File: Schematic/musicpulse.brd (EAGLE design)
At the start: 70.8 x 48.2 mm, 19 parts, among them IC1 UA78M33DCY

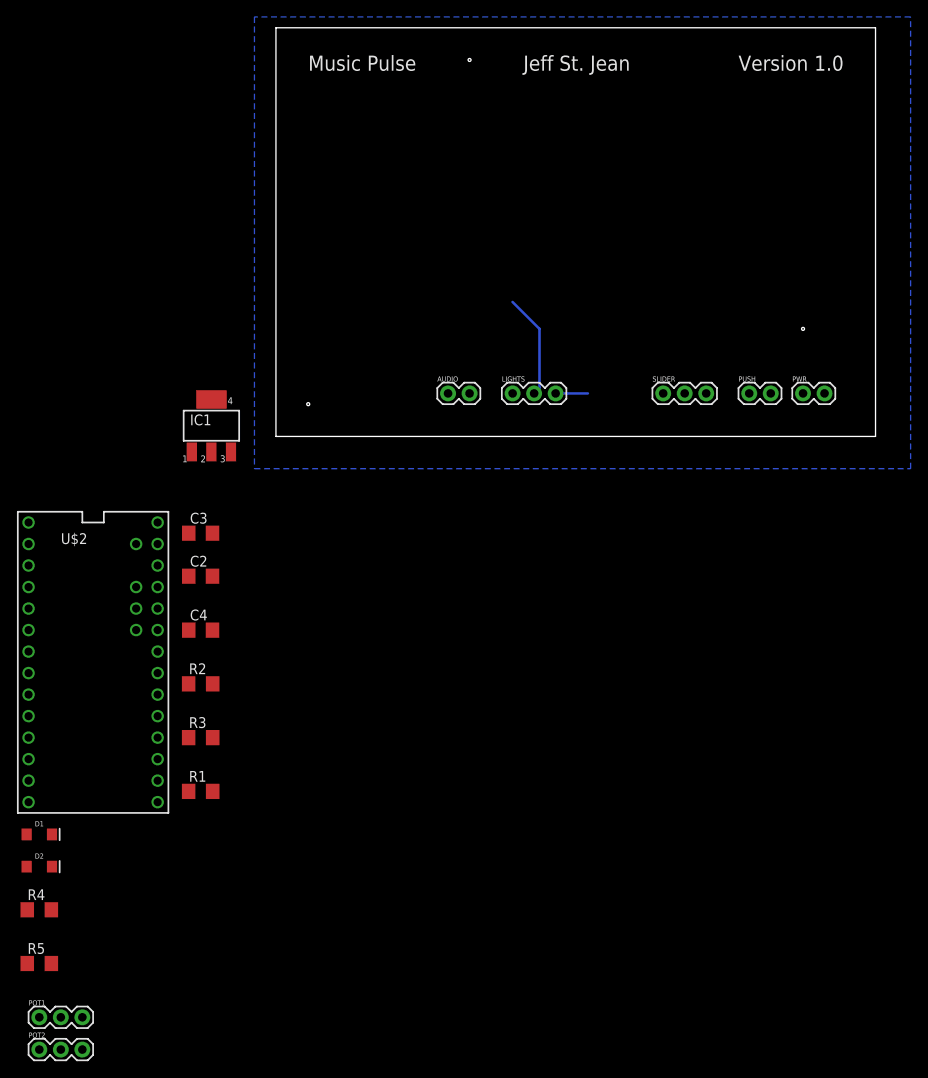
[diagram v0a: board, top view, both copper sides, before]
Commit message: Changed to through hole. Adjusted some resistor files. Rerouted board. Reprocessed gerbers. Added board and schematic reference pictures.
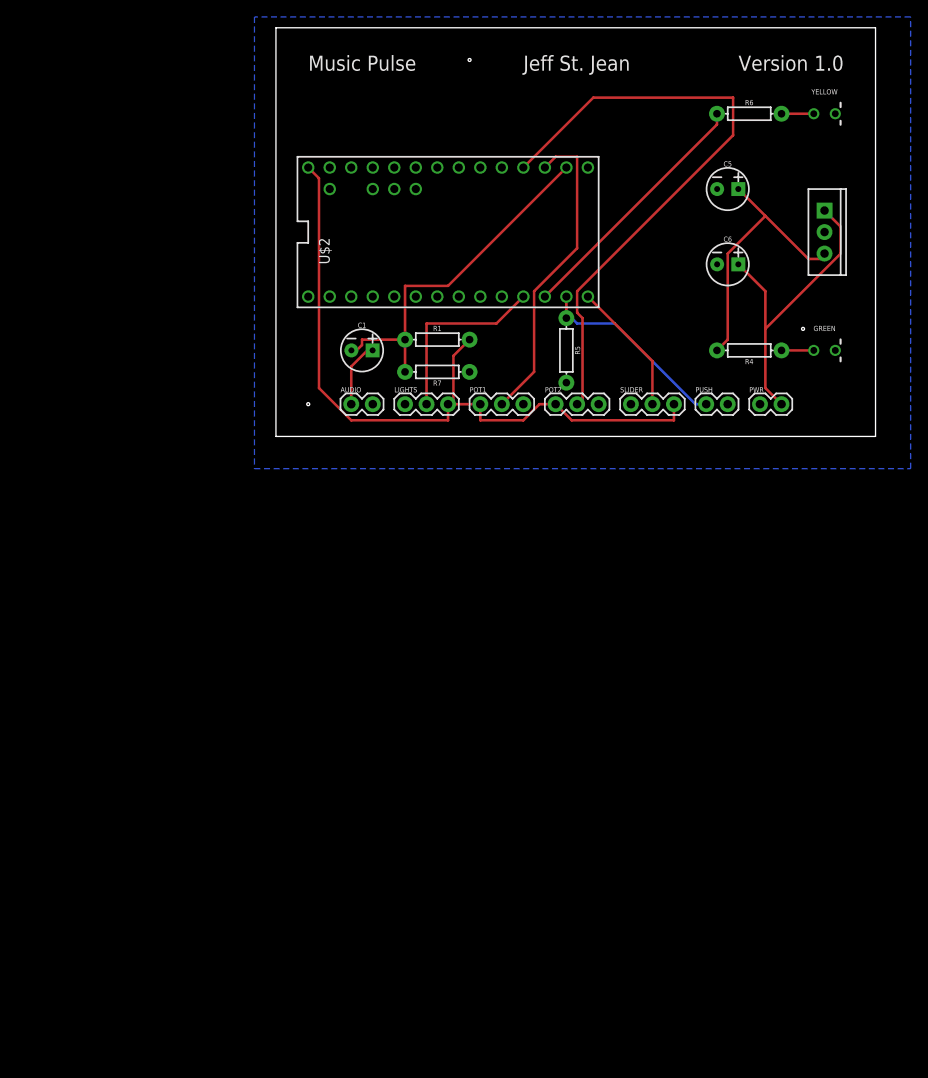
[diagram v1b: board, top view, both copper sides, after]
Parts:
- removed C2: 0.1uF, BeagleBone_Black_Wireless:C1206
- removed C3: 0.33uF, BeagleBone_Black_Wireless:C1206
- removed C4: 10uF, BeagleBone_Black_Wireless:C1206
- removed D1: GREEN, SparkFun-LED:LED-1206
- removed D2: Yellow, SparkFun-LED:LED-1206
- removed IC1: UA78M33DCY, linear:SOT223
- removed R2, R3: 10k, BeagleBone_Black_Wireless:R1206
- added C1: 1uF, SparkFun-Capacitors:CPOL-RADIAL-2.5MM-5MM
- added C5: 0.33uF, SparkFun-Capacitors:CPOL-RADIAL-2.5MM-5MM
- added C6: 0.1uF, SparkFun-Capacitors:CPOL-RADIAL-2.5MM-5MM
- added GREEN, YELLOW: (no value), SparkFun-LED:LED_3MM-NS
- added R6: 100, SparkFun-Resistors:AXIAL-0.3
- added R7: 10K, SparkFun-Resistors:AXIAL-0.3
- added UA7805C: (no value), SparkFun-IC-Power:TO220-IGO
- R1: value 10k -> 4.3K; device BeagleBone_Black_Wireless:R1206 -> SparkFun-Resistors:AXIAL-0.3
- R4: device BeagleBone_Black_Wireless:R1206 -> SparkFun-Resistors:AXIAL-0.3
- R5: value 100 -> 10K; device BeagleBone_Black_Wireless:R1206 -> SparkFun-Resistors:AXIAL-0.3
- moved R4 106.7 mm to (55.9, 10.2), turned to 180 degrees
- moved POT2 97.6 mm to (33.0, 3.81)
- moved R5 95.5 mm to (34.3, 10.2), turned to 270 degrees
- moved POT1 89.2 mm to (24.1, 3.81)
- moved U$2 65.9 mm to (20.3, 24.1), turned to 90 degrees
- moved R1 60.2 mm to (19.1, 11.4)
- moved LIGHTS 12.8 mm to (15.2, 3.81)
- moved AUDIO 11.5 mm to (8.89, 3.81)
- moved PUSH 5.24 mm to (50.8, 3.81)
- moved PWR 5.24 mm to (57.1, 3.81)
- moved SLIDER 4.02 mm to (41.9, 3.81)
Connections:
- net AUDIO_IN: now also C1.2, R1.P$1, R7.P$2; no longer C4.1, R2.2, R3.1
- net GND: now also C5.2, C6.2, GREEN.K, R7.P$1, UA7805C.GND, YELLOW.K; no longer C2.2, C3.2, D1.C, D2.C, IC1.2, IC1.4, R2.1
- net LED_GREEN: now also C5.1, R4.P$2, UA7805C.OUT; no longer C3.1, IC1.3, R4.1
- net LED_YELLOW: now also R6.P$1; no longer R5.2
- net N$1: now also C6.1, UA7805C.IN; no longer C2.1, IC1.1
- net N$2: now also R6.P$2, YELLOW.A; no longer D1.A, R4.2
- net N$3: now also R5.P$2; no longer R1.2
- net N$4: now also GREEN.A, R4.P$1; no longer D2.A, R5.1
- net N$5: now also C1.1; no longer C4.2
- net PUSH: now also R5.P$1; no longer R1.1
- net VCC: now also R1.P$2; no longer R3.2
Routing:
- net VCC: track 3.81 -> 85.8 mm
- net POT2: track 0.00 -> 72.5 mm
- net AUDIO_IN: track 0.00 -> 42.2 mm
- net POT1: track 0.00 -> 37.2 mm
- net N$1: track 0.00 -> 37.1 mm
- net LED_GREEN: track 0.00 -> 32.5 mm
- net LED_YELLOW: track 0.00 -> 30.0 mm
- net PUSH: track 0.00 -> 23.3 mm
- net SLIDE: track 0.00 -> 15.9 mm
- net LIGHTS: track 12.4 -> 22.3 mm
- net N$5: track 0.00 -> 7.75 mm
- net N$4: track 0.00 -> 3.81 mm
- net N$2: track 0.00 -> 3.81 mm

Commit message: Rerouted board. Added pullup to slider. Changed some resistor values.
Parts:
- removed C5: 0.33uF, SparkFun-Capacitors:CPOL-RADIAL-2.5MM-5MM
- added C3: 1uF, SparkFun-Capacitors:CPOL-RADIAL-2.5MM-5MM
- added R3: 330, SparkFun-Resistors:AXIAL-0.3
- C1: value 1uF -> 0.1uF
- C2: value 0.1uF -> 0.33uF
- R4: value 100 -> 330
- R6: value 100 -> 10K
- U$2: value TEENSY_3.1-3.2_DIL+4 -> TEENSY_3.2
- moved C1 46.7 mm to (53.3, 27.9)
- moved PWR 29.6 mm to (52.1, 33.0)
- moved R6 28.1 mm to (48.4, 11.0), turned to 270 degrees
- moved YELLOW 27.9 mm to (45.7, 17.8), turned to 180 degrees
- moved R4 15.8 mm to (46.6, 23.0), turned to 0 degrees
- moved PUSH 8.89 mm to (41.9, 3.81)
- moved SLIDER 6.35 mm to (48.3, 3.81)
- turned R5 to 180 degrees
- renumbered C6 to C2, R7 to R2
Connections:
- removed net LED_GREEN: C5.1, R4.P$2, UA7805C.OUT
- net AUDIO_IN: now also C3.2; no longer C1.2
- net GND: now also C1.2; no longer C5.2
- net LED_YELLOW: now also R4.P$1; no longer R6.P$1
- net N$1: now also C1.1; no longer C2.1
- net N$2: now also R4.P$2; no longer R6.P$2
- net N$4: now also R3.P$1; no longer R4.P$1
- net N$5: now also C3.1; no longer C1.1
- net SLIDE: now also R6.P$2
- net VCC: now also C2.1, R3.P$2, R6.P$1, UA7805C.OUT
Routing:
- net VCC: track 85.8 -> 125.4 mm
- net LED_GREEN: track 32.5 -> 0.00 mm
- net AUDIO_IN: track 42.2 -> 68.0 mm
- net N$1: track 37.1 -> 15.8 mm
- net LED_YELLOW: track 30.0 -> 13.7 mm
- net POT1: track 37.2 -> 45.5 mm
- net SLIDE: track 15.9 -> 23.7 mm
- net PUSH: track 23.3 -> 15.9 mm
- net N$2: track 3.81 -> 6.63 mm
- net LIGHTS: track 22.3 -> 19.6 mm
- net N$5: track 7.75 -> 6.36 mm
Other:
- board size 70.8 x 48.2 mm -> 70.8 x 41.9 mm
- board text added: "Music Kaleidoscope"
- board text removed: "Music Pulse"

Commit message: Added missing trace. Reprocessed CAM files.
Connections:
- removed net N$3: R5.P$2
- net VCC: now also R5.P$2
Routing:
- net VCC: track 125.4 -> 131.5 mm
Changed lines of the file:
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@@
 </element>
 <element name="R4" library="SparkFun-Resistors" library_urn="urn:adsk.eagle:library:532" package="AXIAL-0.3" package3d_urn="urn:adsk.eagle:package:39658/1" value="330" x="46.609" y="22.987" smashed="yes">
-<attribute name="NAME" x="46.609" y="24.003" size="0.6096" layer="25" font="vector" ratio="20" align="bottom-center"/>
+<attribute name="NAME" x="46.609" y="21.463" size="0.6096" layer="25" font="vector" ratio="20" align="bottom-center"/>
 <attribute name="PROD_ID" value="RES-12182" x="46.609" y="22.987" size="1.778" layer="27" display="off"/>
-<attribute name="VALUE" x="46.609" y="21.971" size="0.6096" layer="27" font="vector" ratio="20" align="top-center"/>
+<attribute name="VALUE" x="46.609" y="24.511" size="0.6096" layer="27" font="vector" ratio="20" align="top-center"/>
 </element>
 <element name="R3" library="SparkFun-Resistors" library_urn="urn:adsk.eagle:library:532" package="AXIAL-0.3" package3d_urn="urn:adsk.eagle:package:39658/1" value="330" x="55.88" y="10.16" smashed="yes" rot="R180">
@@
 </element>
 <element name="R1" library="SparkFun-Resistors" library_urn="urn:adsk.eagle:library:532" package="AXIAL-0.3" package3d_urn="urn:adsk.eagle:package:39658/1" value="4.3K" x="19.05" y="11.43" smashed="yes">
-<attribute name="NAME" x="19.05" y="12.446" size="0.6096" layer="25" font="vector" ratio="20" align="bottom-center"/>
+<attribute name="NAME" x="19.05" y="9.906" size="0.6096" layer="25" font="vector" ratio="20" align="bottom-center"/>
 <attribute name="PROD_ID" value="RES-12182" x="19.05" y="11.43" size="1.778" layer="27" display="off"/>
-<attribute name="VALUE" x="19.05" y="10.414" size="0.6096" layer="27" font="vector" ratio="20" align="top-center"/>
+<attribute name="VALUE" x="19.05" y="12.954" size="0.6096" layer="27" font="vector" ratio="20" align="top-center"/>
 </element>
 <element name="R2" library="SparkFun-Resistors" library_urn="urn:adsk.eagle:library:532" package="AXIAL-0.3" package3d_urn="urn:adsk.eagle:package:39658/1" value="10K" x="19.05" y="7.62" smashed="yes" rot="R180">
@@
 <wire x1="22.86" y1="11.43" x2="24.13" y2="11.43" width="0.3048" layer="16"/>
 <wire x1="24.13" y1="11.43" x2="25.4" y2="10.16" width="0.3048" layer="16"/>
-<wire x1="25.4" y1="10.16" x2="25.4" y2="5.08" width="0.3048" layer="16"/>
+<wire x1="25.4" y1="10.16" x2="25.4" y2="7.62" width="0.3048" layer="16"/>
+<wire x1="25.4" y1="7.62" x2="25.4" y2="5.08" width="0.3048" layer="16"/>
 <wire x1="25.4" y1="5.08" x2="24.13" y2="3.81" width="0.3048" layer="16"/>
 <wire x1="22.86" y1="11.43" x2="20.32" y2="13.97" width="0.3048" layer="1"/>
@@
 <wire x1="48.387" y1="14.859" x2="49.149" y2="14.859" width="0.3048" layer="1"/>
 <wire x1="49.149" y1="14.859" x2="52.07" y2="17.78" width="0.3048" layer="1"/>
+<contactref element="R5" pad="P$2"/>
+<wire x1="30.48" y1="10.16" x2="27.94" y2="10.16" width="0.3048" layer="16"/>
+<wire x1="27.94" y1="10.16" x2="25.4" y2="7.62" width="0.3048" layer="16"/>
 </signal>
 <signal name="LIGHTS">
@@
 <wire x1="43.18" y1="20.32" x2="31.75" y2="31.75" width="0.3048" layer="1"/>
 </signal>
-<signal name="N$3">
-<contactref element="R5" pad="P$2"/>
-</signal>
 <signal name="N$2">

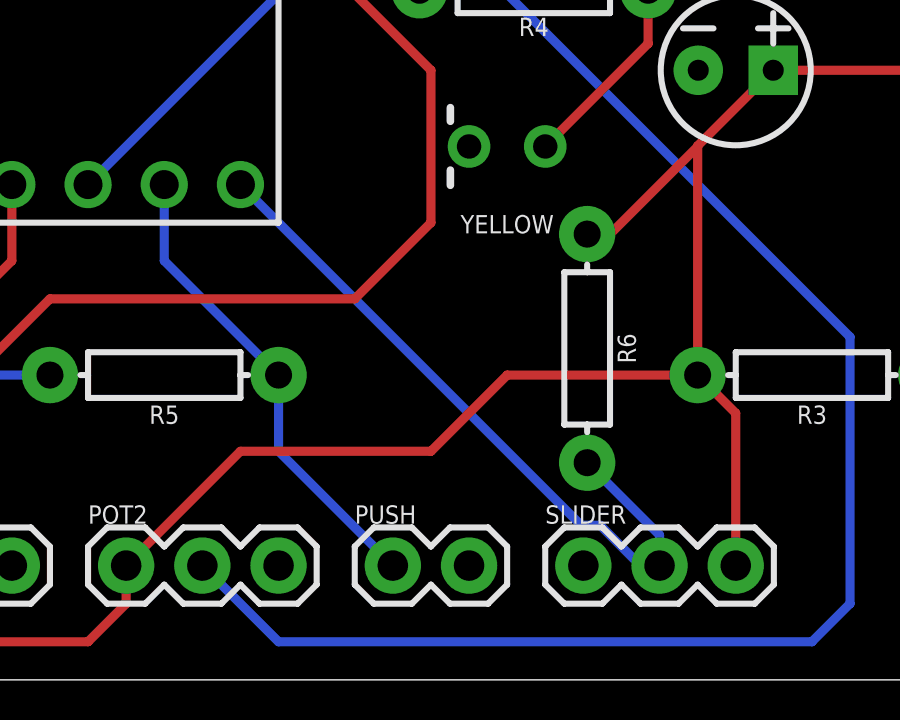
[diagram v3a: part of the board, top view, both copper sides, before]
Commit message: Adjusted slider trace
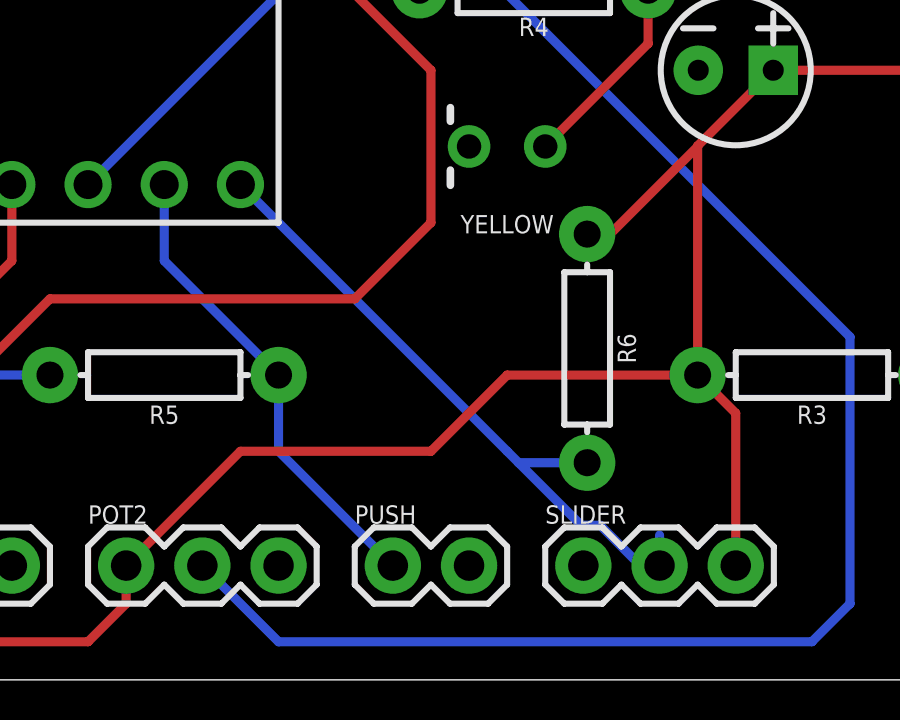
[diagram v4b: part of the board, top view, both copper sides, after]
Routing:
- net SLIDE: track 23.7 -> 22.5 mm
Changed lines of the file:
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@@
 <contactref element="U$2" pad="12"/>
 <wire x1="48.81761875" y1="5.1562" x2="48.1838" y2="5.1562" width="0.3048" layer="16"/>
-<wire x1="48.1838" y1="5.1562" x2="36.83" y2="16.51" width="0.3048" layer="16"/>
+<wire x1="48.1838" y1="5.1562" x2="46.101" y2="7.239" width="0.3048" layer="16"/>
+<wire x1="45.72" y1="7.62" x2="36.83" y2="16.51" width="0.3048" layer="16"/>
 <wire x1="50.8" y1="3.81" x2="50.16381875" y2="3.81" width="0.3048" layer="16"/>
 <wire x1="50.16381875" y1="3.81" x2="48.81761875" y2="5.1562" width="0.3048" layer="16"/>
 <contactref element="R6" pad="P$2"/>
-<wire x1="48.387" y1="7.239" x2="50.8" y2="4.826" width="0.3048" layer="16"/>
 <wire x1="50.8" y1="4.826" x2="50.8" y2="3.81" width="0.3048" layer="16"/>
+<wire x1="48.387" y1="7.239" x2="46.101" y2="7.239" width="0.3048" layer="16"/>
+<wire x1="46.101" y1="7.239" x2="45.72" y2="7.62" width="0.3048" layer="16"/>
 </signal>
 <signal name="N$1">
